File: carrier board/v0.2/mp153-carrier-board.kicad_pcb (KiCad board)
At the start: 2 copper layers, 87.2 x 87.4 mm, 92 parts, among them J1 USB-C_Receptacle_Molex_217179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, J10 3.5mm_Mono_Switched_sm, J11 3.5mm_Mono_Switched_sm, J12 3.5mm_Mono_Switched_sm, J13 3.5mm_Mono_Switched_sm, J4 Socket_02x40_P0.4mm_W3.0mm_SMT, J5 3.5mm_Mono_Switched_sm, J6 Socket_02x40_P0.4mm_W3.0mm_SMT, J7 Eurorack_Power_16pin_Unshroud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, J9 3.5mm_Mono_Switched_sm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

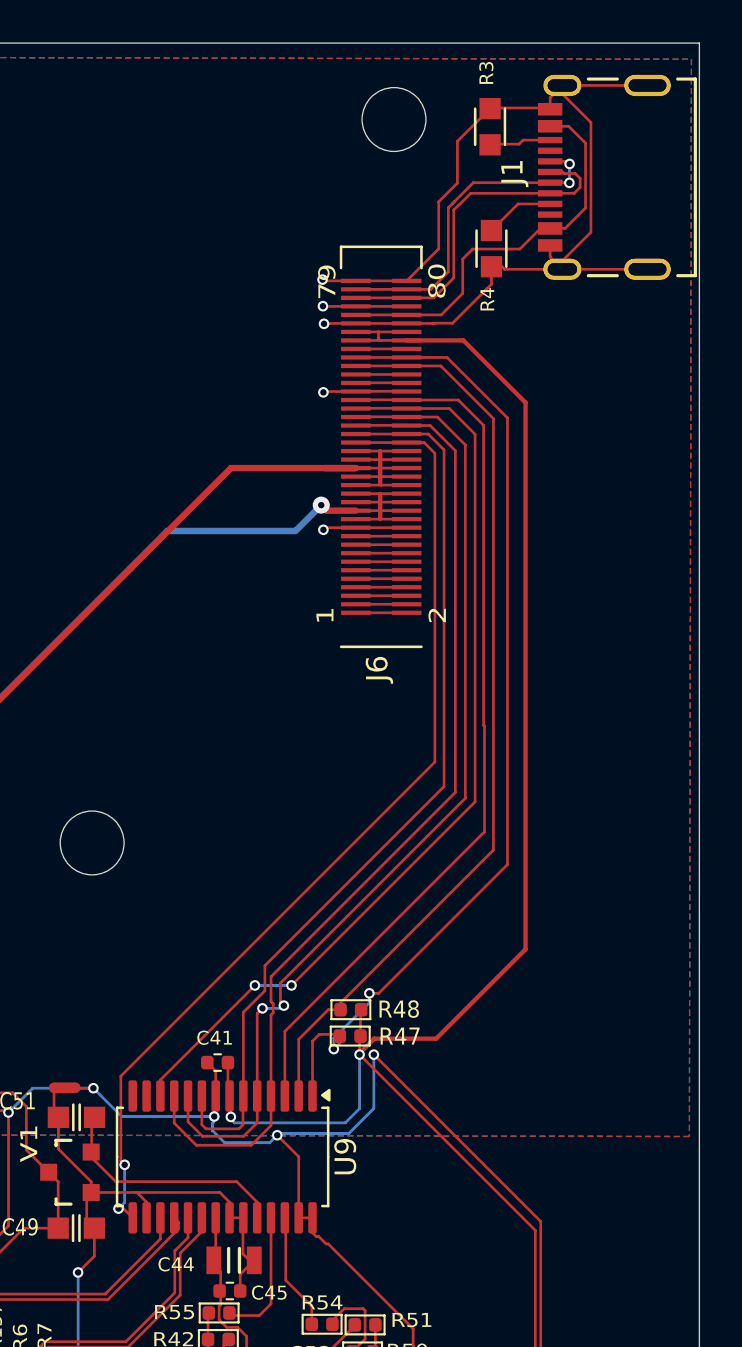
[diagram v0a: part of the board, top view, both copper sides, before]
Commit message: Move carrier board to v0.1 dir. Rename p2=>v0.2
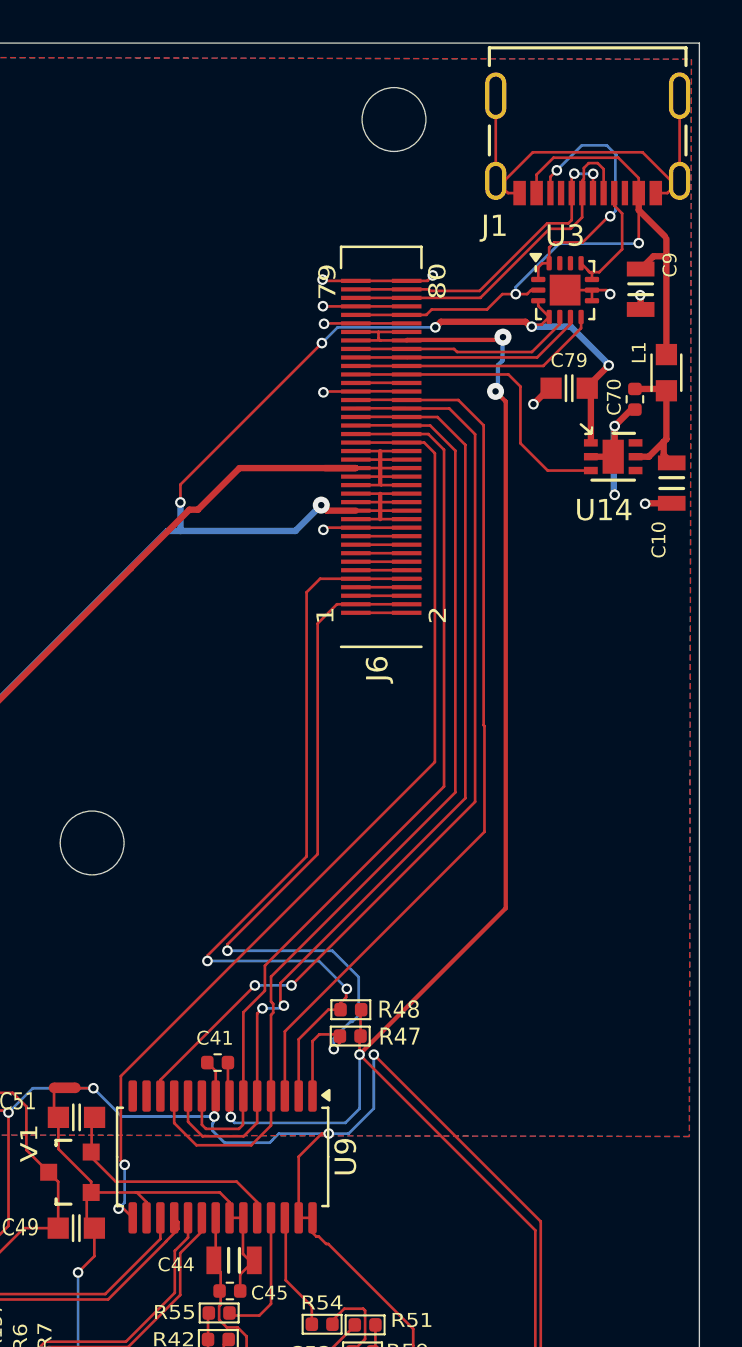
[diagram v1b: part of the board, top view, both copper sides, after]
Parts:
- removed R3, R4: 5.1k_0603, 4ms_Resistor:R_0603
- added C10: 10uF_0805_16V_lowESR, 4ms_Capacitor:C_0805, F.Cu at (250.7, 95.8)
- added C70: 4.7uF_0402_6.3V, 4ms_Capacitor:C_0402, F.Cu at (249.0, 91.9)
- added C79: 22uF_0603_6.3V, 4ms_Capacitor:C_0603, F.Cu at (245.9, 91.4)
- added C9: 10uF_0805_16V_lowESR, 4ms_Capacitor:C_0805, F.Cu at (249.3, 86.7)
- added L1: FerriteBead_0603_0.8A_300mΩ, 4ms_Resistor:R_0603, F.Cu at (250.5, 90.6)
- added U14: AP2411SN, 4ms_Package_QFP:DFN-6-1EP_2x2mm_P0.65mm_EP1x1.6mm, F.Cu at (248.0, 94.6)
- added U3: FUSB302BMPX, Package_DFN_QFN:WQFN-14-1EP_2.5x2.5mm_P0.5mm_EP1.45x1.45mm, F.Cu at (245.7, 86.8)
- moved J1 3.16 mm to (246.8, 78.8), turned to 180 degrees
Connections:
- J1 pad A5: Net-(J1-CC1) -> /CC1
- J1 pad B5: Net-(J1-CC2) -> /CC2
- R47 pad 1: /D5 -> /D10
- R48 pad 1: /D21 -> /D17
- U9 pad 1: /D5 -> /D10
- U9 pad 2: /D21 -> /D17
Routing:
- net /D17: track 3.06 -> 38.5 mm, vias 0 -> 2
- net /D5: track 46.4 -> 11.1 mm, vias 2 -> 0
- net /D10: track 2.39 -> 37.1 mm, vias 0 -> 2
- net +5V: track 76.8 -> 109.2 mm, vias 2 -> 7
- net /D21: track 43.6 -> 11.9 mm
- net /USB_VBUS_JACK: track 18.9 -> 35.0 mm, vias 0 -> 2
- net /CC2: track 0.00 -> 13.0 mm, vias 0 -> 2
- net /D24: track 2.39 -> 14.5 mm
- net /D11: track 2.39 -> 10.5 mm
- net GND: track 595.5 -> 588.5 mm, vias 22 -> 29
- net /USBSW_5V: track 0.00 -> 6.73 mm
- net /CC1: track 0.00 -> 5.73 mm
- net Net-(J1-CC1): track 3.28 -> 0.00 mm
- net Net-(J1-CC2): track 2.92 -> 0.00 mm
- net +3V3: track 173.2 -> 172.4 mm, vias 4 -> 6
